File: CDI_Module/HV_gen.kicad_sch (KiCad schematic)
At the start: 0 parts

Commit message: First Drawing of High volatage generator part
First Drawing of High volatage generator part
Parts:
- added C2: 500V / 5uF, symbol Device:C
- added C3: 1nF, Capacitor_THT:C_Axial_L5.1mm_D3.1mm_P10.00mm_Horizontal, symbol Device:C
- added C4: 10nF, Capacitor_THT:C_Axial_L5.1mm_D3.1mm_P10.00mm_Horizontal, symbol Device:C
- added D2: 1N4007, Diode_THT:D_DO-41_SOD81_P10.16mm_Horizontal, symbol Diode:1N4007
- added L1: 100mH, symbol Device:L
- added Q2: IRF3205, Package_TO_SOT_THT:TO-220-3_Vertical, symbol Transistor_FET:IRF3205
- added R3, R5: 1k, Resistor_THT:R_Axial_DIN0204_L3.6mm_D1.6mm_P5.08mm_Horizontal, symbol Device:R
- added R4: 75k, Resistor_THT:R_Axial_DIN0204_L3.6mm_D1.6mm_P5.08mm_Horizontal, symbol Device:R
- added U1: NE555P, Package_DIP:DIP-8_W7.62mm, symbol Timer:NE555P
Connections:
- new net: D2.2 (A), L1.2, Q2.2 (D)
- new net: C4.1, U1.5 (CV)
- new net: R3.2, R4.1, U1.7 (DIS)
- new net: C3.1, R4.2, U1.2 (TR), U1.6 (THR)
- new net +12V: L1.1, R3.1, U1.4 (R), U1.8 (VCC)
- new net GND: C2.2, C3.2, C4.2, Q2.3 (S), R5.2, U1.1 (GND)
- new net HT: C2.1, D2.1 (K)
- new net PULSE: Q2.1 (G), R5.1, U1.3 (Q)
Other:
- note added: "Dimentionnement oscillateur : VOut = 10,5V f = 9,554 kHz Duty Cycle = 50,331% T = 104 us"

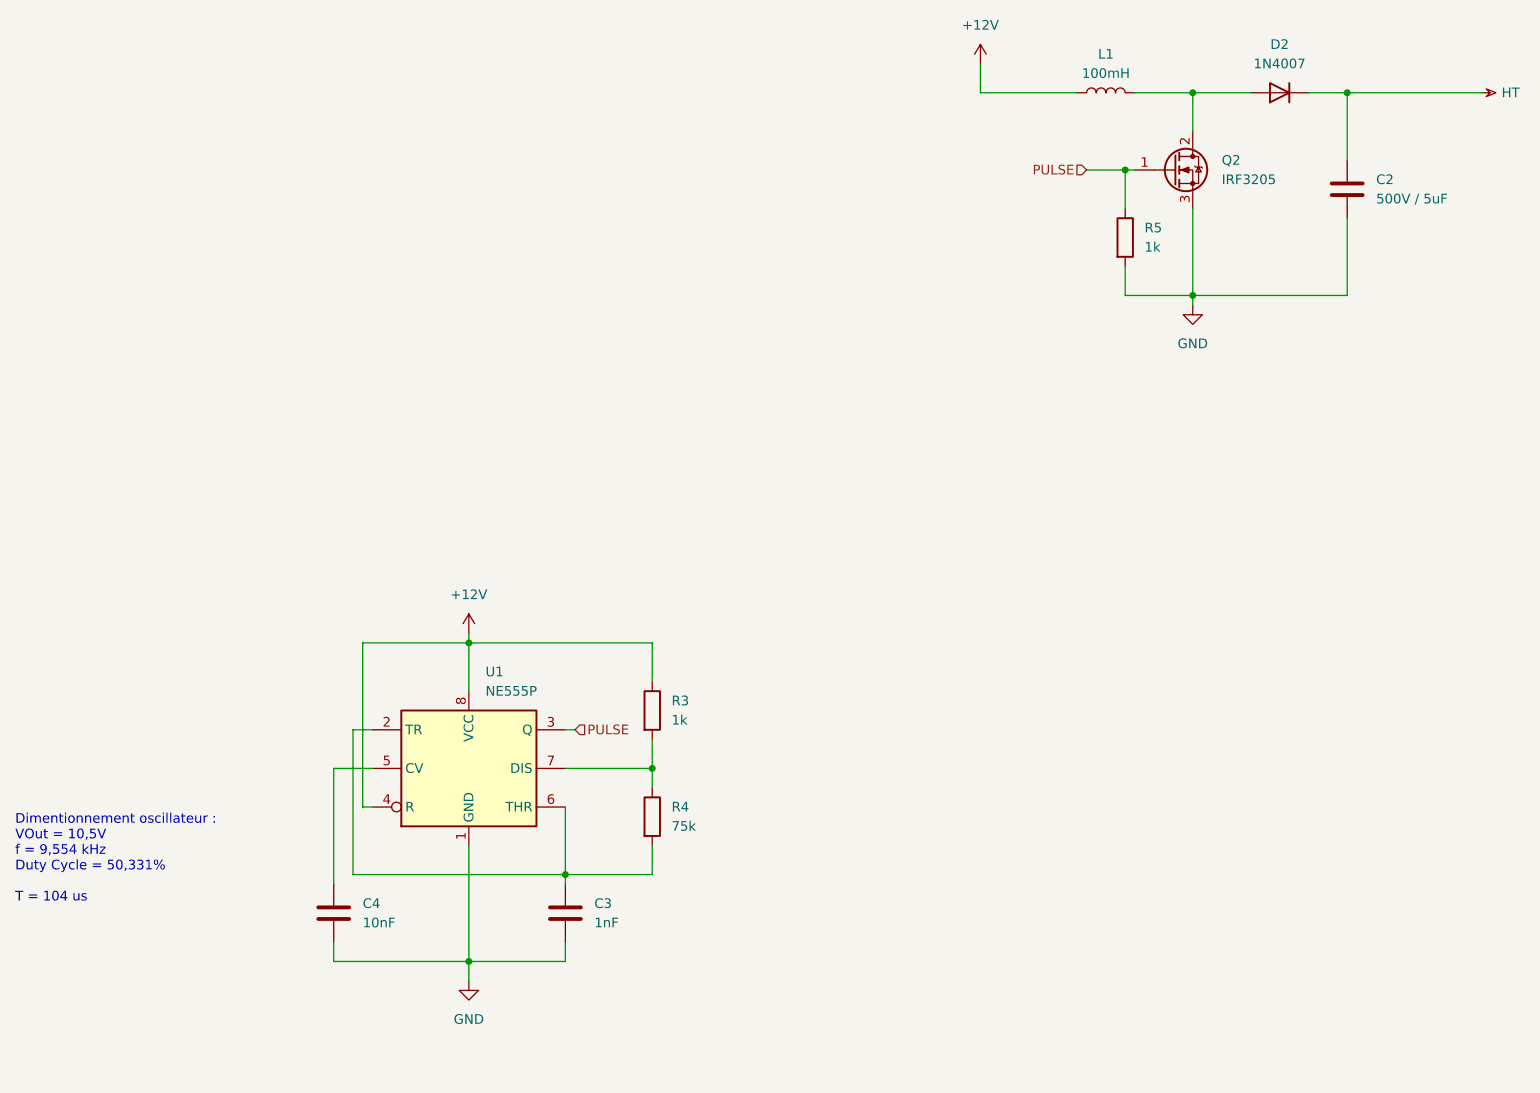
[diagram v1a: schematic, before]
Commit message: Changed Connectors for Molex CMC 48pins Black.
Changed ECU Connector for Molex CMC 48pins Black, for compacity and cost reduction. Designed custom Footprint for this purpose
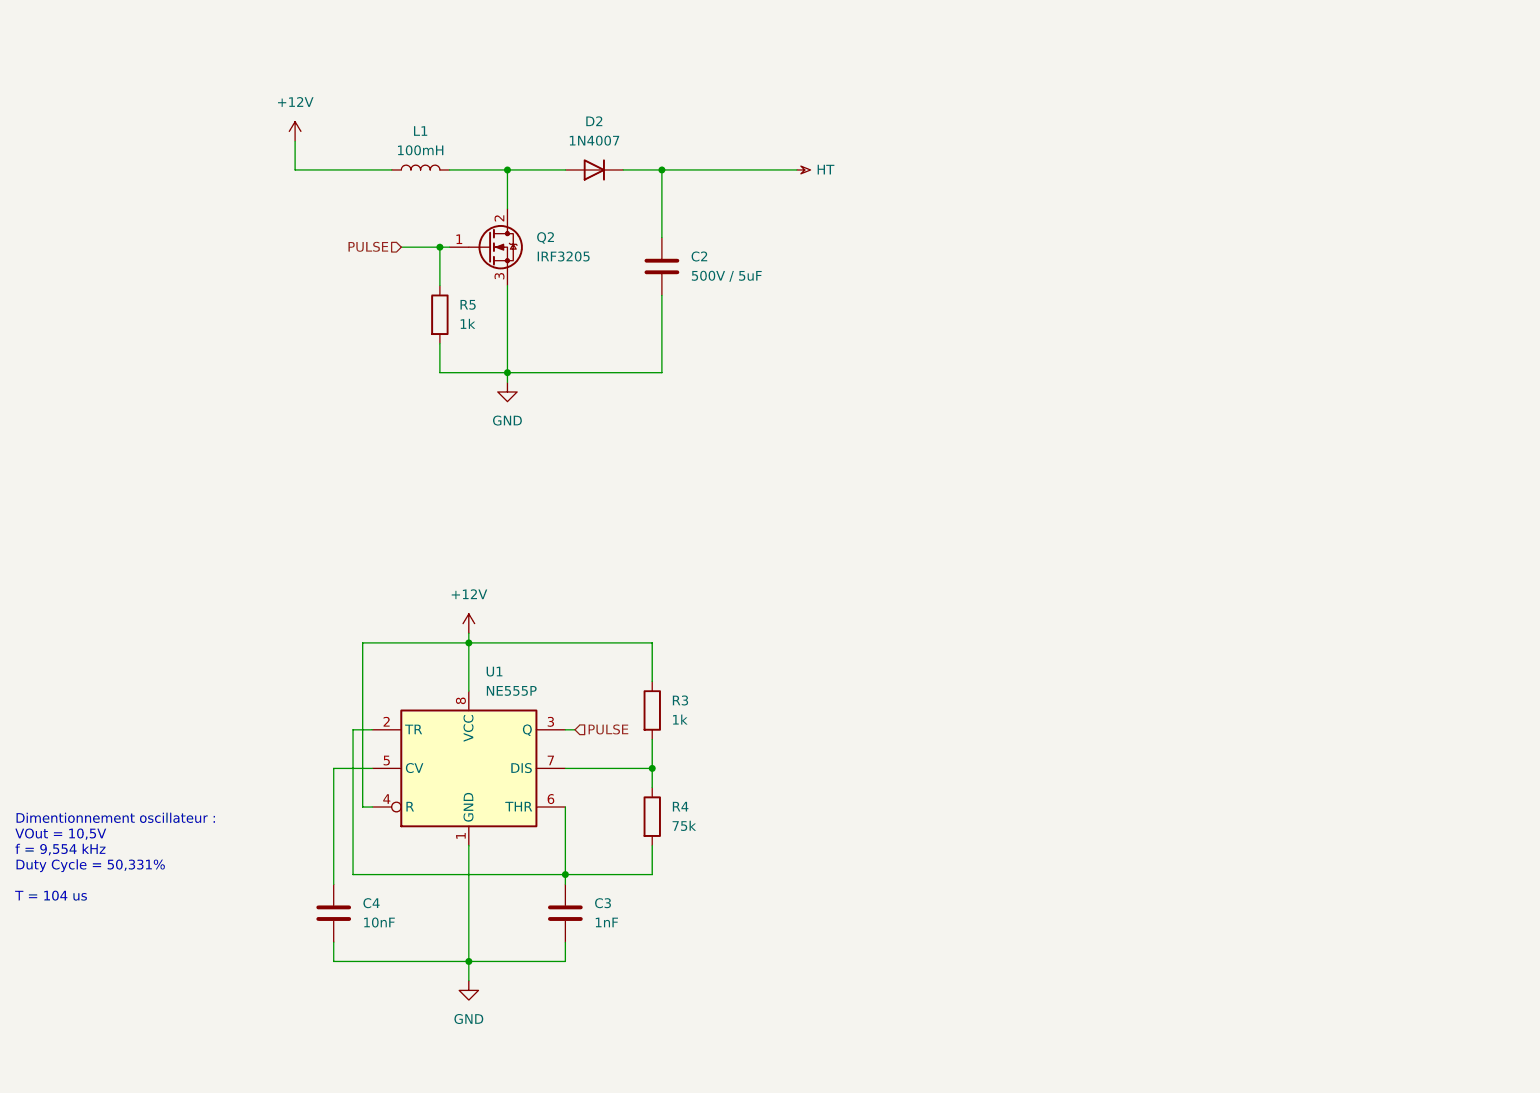
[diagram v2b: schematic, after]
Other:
- moved on the sheet: C2, D2, L1, Q2, R5

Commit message: Test montage générateur de Haute tension
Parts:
- added C6, C7, C8, C9: ?, symbol Device:C
- added D4, D5, D6, D7: 1N4007, Diode_THT:D_DO-41_SOD81_P10.16mm_Horizontal, symbol Diode:1N4007
- added Q4: Q_NPN_EBC, symbol Device:Q_NPN_EBC
- added R9: 1k, Resistor_THT:R_Axial_DIN0204_L3.6mm_D1.6mm_P5.08mm_Horizontal, symbol Device:R
- C2: value 500V / 5uF -> 5uF
- R5: value 1k -> 100K
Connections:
- net +12V: now also Q4.3 (C)
- net GND: now also C9.2, D6.2 (A), R9.2; no longer C2.2, Q2.3 (S)
- net HT: now also C8.1, D7.1 (K); no longer C2.1, D2.1 (K)
- net PULSE: now also Q4.2 (B), R9.1; no longer Q2.1 (G), R5.1
- new net: C2.2, C8.2, C9.1, D4.2 (A), D5.1 (K), Q2.3 (S)
- new net: C6.1, D4.1 (K), D7.2 (A)
- new net: Q2.1 (G), Q4.1 (E), R5.1
- new net: C2.1, C6.2, C7.1, D2.1 (K)
- new net: C7.2, D5.2 (A), D6.1 (K)
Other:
- moved on the sheet: C2, C3, C4, D2, L1, Q2, R3, R4, R5, U1
